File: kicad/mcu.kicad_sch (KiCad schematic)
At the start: 17 parts, among them J2 Conn_ARM_SWD_TagConnect_TC2030, SW1 SW_Push, U1 ESP32-C6-MINI-1/U

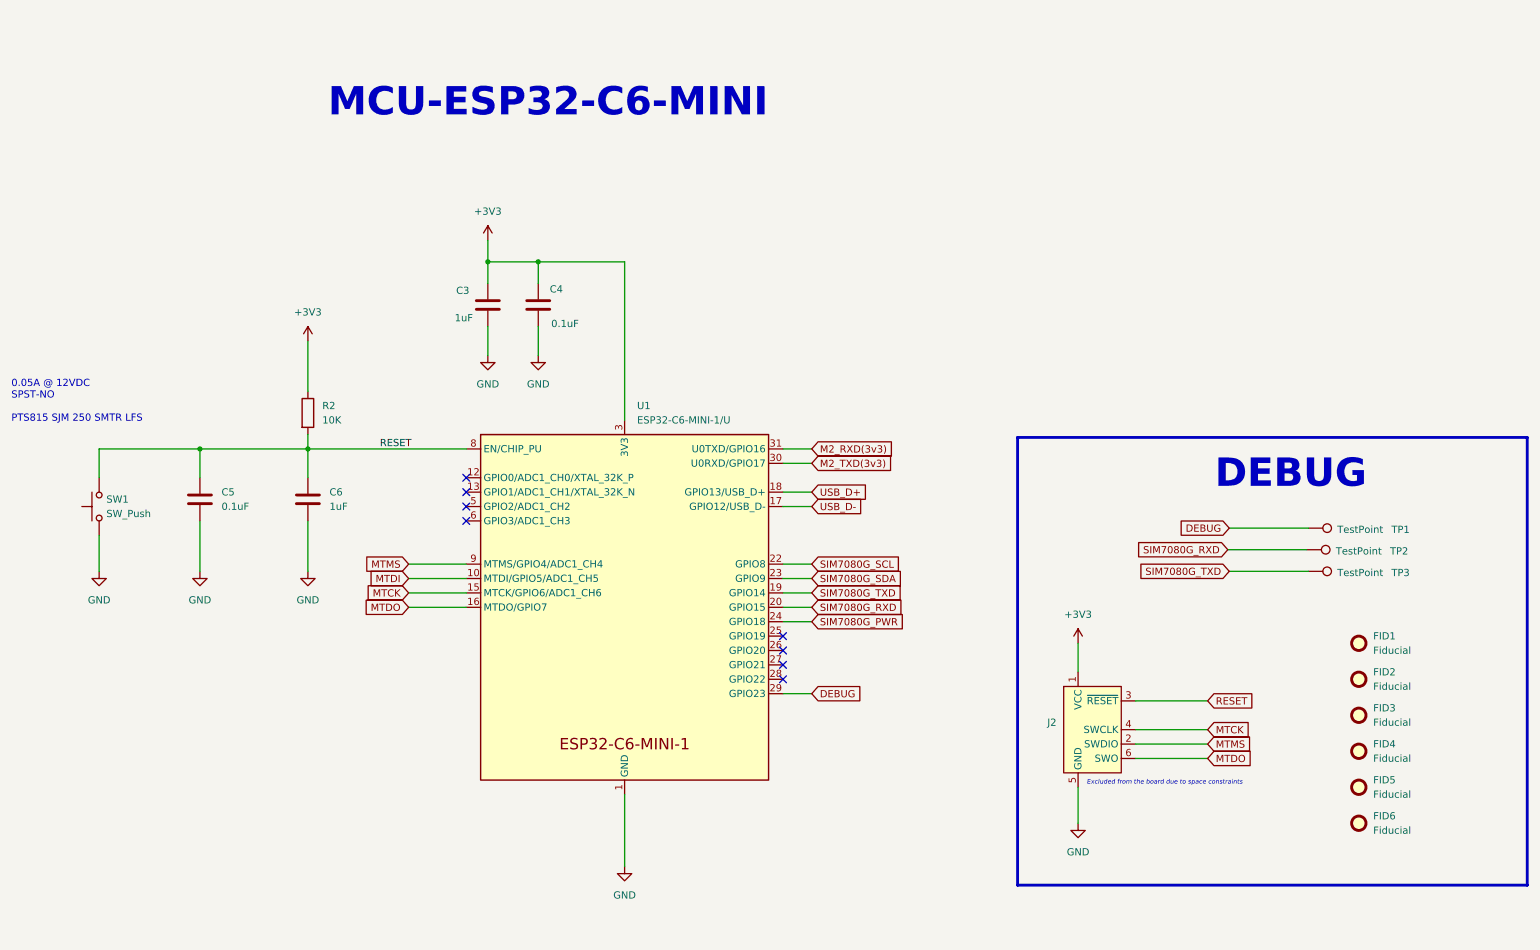
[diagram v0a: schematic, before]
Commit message: feat: minimal module with compute alone
Signed-off-by: Rodney Osodo <socials@rodneyosodo.com>
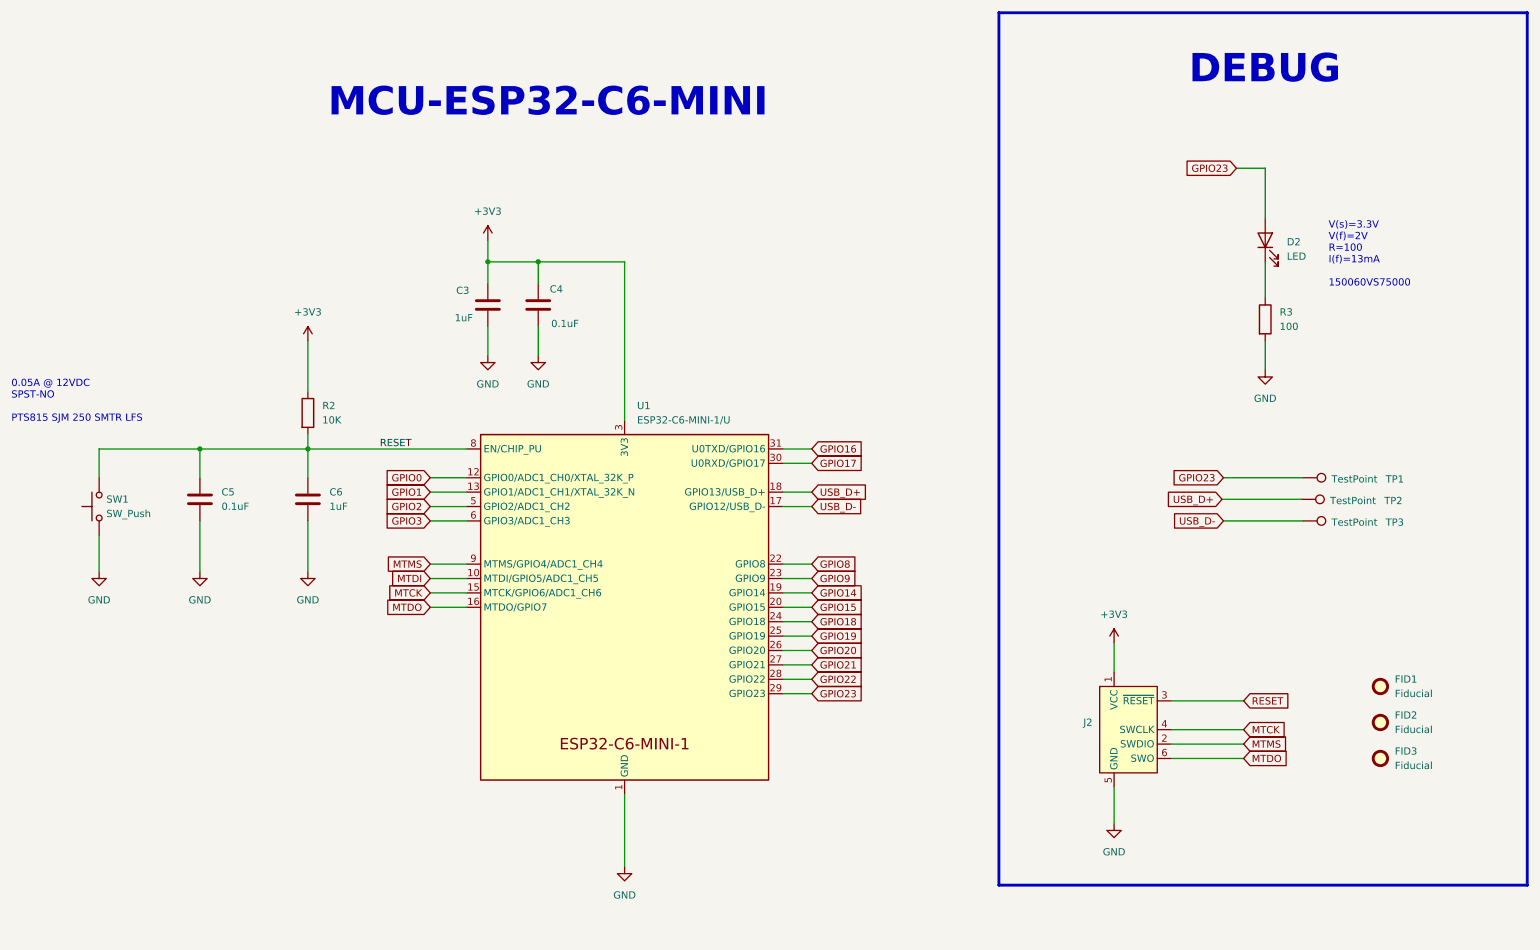
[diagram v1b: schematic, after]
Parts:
- removed FID4, FID5, FID6: Fiducial, Fiducial:Fiducial_0.5mm_Mask1mm, symbol Mechanical:Fiducial
- removed J2: Conn_ARM_SWD_TagConnect_TC2030, Connector:Tag-Connect_TC2030-IDC-FP_2x03_P1.27mm_Vertical, symbol Connector:Conn_ARM_SWD_TagConnect_TC2030
- added D2: LED, LED_SMD:LED_0603_1608Metric, symbol Device:LED
- added J2: Conn_ARM_SWD_TagConnect_TC2030-NL, Connector:Tag-Connect_TC2030-IDC-NL_2x03_P1.27mm_Vertical, symbol Connector:Conn_ARM_SWD_TagConnect_TC2030-NL
- added R3: 100, Resistor_SMD:R_0603_1608Metric, symbol Device:R
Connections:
- net +3V3: now also J2.1 (VCC)
- net GND: now also J2.5 (GND), R3.2
- net MTCK: now also J2.4 (SWCLK)
- net MTDO: now also J2.6 (SWO)
- net MTMS: now also J2.2 (SWDIO)
- net RESET: now also J2.3 (~{RESET})
- net USB_D+: now also TP2.1
- net USB_D-: now also TP3.1
- net GPIO0: now reaches U1.12 (GPIO0/ADC1_CH0/XTAL_32K_P)
- net GPIO1: now reaches U1.13 (GPIO1/ADC1_CH1/XTAL_32K_N)
- net GPIO19: now reaches U1.25 (GPIO19)
- net GPIO20: now reaches U1.26 (GPIO20)
- net GPIO21: now reaches U1.27 (GPIO21)
- net GPIO22: now reaches U1.28 (GPIO22)
- net GPIO2: now reaches U1.5 (GPIO2/ADC1_CH2)
- net GPIO3: now reaches U1.6 (GPIO3/ADC1_CH3)
- net DEBUG renamed GPIO23
- net GPIO23: now also D2.2 (A)
- net M2_RXD(3v3) renamed GPIO16
- net M2_TXD(3v3) renamed GPIO17
- net SIM7080G_PWR renamed GPIO18
- net SIM7080G_RXD renamed GPIO15
- net GPIO15: no longer TP2.1
- net SIM7080G_SCL renamed GPIO8
- net SIM7080G_SDA renamed GPIO9
- net SIM7080G_TXD renamed GPIO14
- net GPIO14: no longer TP3.1
- new net: D2.1 (K), R3.1
- no-connect marks 8 -> 0
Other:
- note added: "V(s)=3.3V V(f)=2V R=100 I(f)=13mA 150060VS75000"
- note removed: "Excluded from the board due to space constraints"
- moved on the sheet: FID1, FID2, FID3, TP1, TP2, TP3

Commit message: refactor: change to JLCPCB as production and assembly
Signed-off-by: Rodney Osodo <socials@rodneyosodo.com>
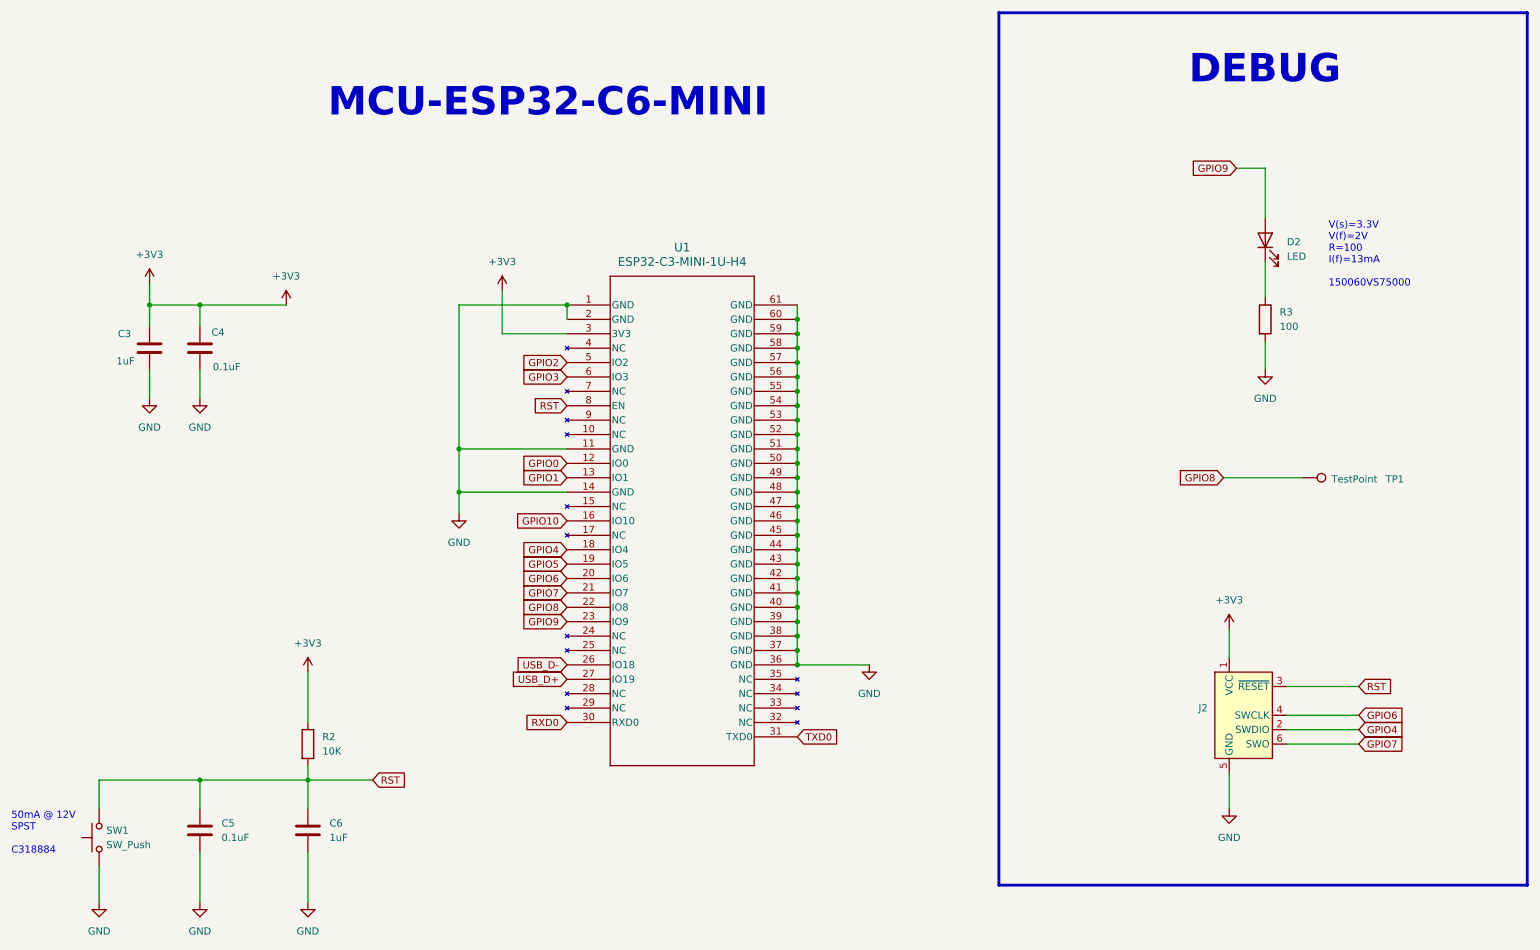
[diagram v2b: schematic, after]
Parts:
- removed FID1, FID2, FID3: Fiducial, Fiducial:Fiducial_0.5mm_Mask1mm, symbol Mechanical:Fiducial
- removed TP2, TP3: TestPoint, TestPoint:TestPoint_Pad_D1.0mm, symbol Connector:TestPoint
- removed U1: ESP32-C6-MINI-1/U, PCM_Espressif:ESP32-C6-MINI-1U, symbol PCM_Espressif:ESP32-C6-MINI-1/U
- added U1: ESP32-C3-MINI-1U-H4, ESP32-C3-MINI-1U-H4:ESP32-C3-MINI-1U_EXP, symbol 2024-11-20_06-36-54:ESP32-C3-MINI-1U-H4
- SW1: footprint tactile-switch:SW4_PTS815 SJM 250 SMTR LFS_CNK -> Switch:TS-1187A-B-A-B_XKB
- TP1: now left out of the parts list
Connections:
- net +3V3: now also U1.3 (3V3)
- net GND: now also U1.1 (GND), U1.11 (GND), U1.14 (GND), U1.2 (GND), U1.36 (GND), U1.37 (GND), U1.38 (GND), U1.39 (GND), U1.40 (GND), U1.41 (GND), U1.42 (GND), U1.43 (GND), U1.44 (GND), U1.45 (GND), U1.46 (GND), U1.47 (GND), U1.48 (GND), U1.49 (GND), U1.50 (GND), U1.51 (GND), U1.52 (GND), U1.53 (GND), U1.54 (GND), U1.55 (GND), U1.56 (GND), U1.57 (GND), U1.58 (GND), U1.59 (GND), U1.60 (GND), U1.61 (GND)
- net GPIO0: now also U1.12 (IO0)
- net GPIO1: now also U1.13 (IO1)
- net GPIO2: now also U1.5 (IO2)
- net GPIO3: now also U1.6 (IO3)
- net GPIO8: now also TP1.1, U1.22 (IO8)
- net GPIO9: now also D2.2 (A), U1.23 (IO9)
- net USB_D+: now also U1.27 (IO19)
- net USB_D-: now also U1.26 (IO18)
- removed net GPIO23: D2.2 (A), TP1.1
- net MTCK renamed GPIO6
- net GPIO6: now also U1.20 (IO6)
- net MTDO renamed GPIO7
- net GPIO7: now also U1.21 (IO7)
- net MTMS renamed GPIO4
- net GPIO4: now also U1.18 (IO4)
- net RESET renamed RST
- net RST: now also U1.8 (EN)
- new net GPIO10: U1.16 (IO10)
- new net GPIO5: U1.19 (IO5)
- new net RXD0: U1.30 (RXD0)
- new net TXD0: U1.31 (TXD0)
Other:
- note added: "50mA @ 12V SPST C318884"
- note removed: "0.05A @ 12VDC SPST-NO PTS815 SJM 250 SMTR LFS"
- moved on the sheet: C3, C4, C5, C6, J2, R2, SW1
